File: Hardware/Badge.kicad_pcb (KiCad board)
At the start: 2 copper layers, 100 x 100 mm, 128 parts, among them IC2 ST25DV04K-IER6S3, J1 Battery_Conn, J4 Conn_02x15_Counter_Clockwise, J5 Conn_01x12, J6 Internal_I2C, P1 USB_C_Plug_USB2.0, P2 ESP_DATA, Q1 SI1967DH-T1-GE3, Q2 2SC4213, SW1 BOOT_MODE, SW2 RESET, SW3 PWR_BATT, SW4 ESP_BOOT, SW5 Button B, SW6 Button A, SW7 ESP_RST, U1 W25Q128JVS, U2 MCP73832-2-OT, U3 LD1117S33TR_SOT223, U4 RP2040, U5 BHI160B, U6 BMM150, U7 ESP32-S3-WROOM-1, X1 Simple_Addon_v2, Y1 12MHz_GND24

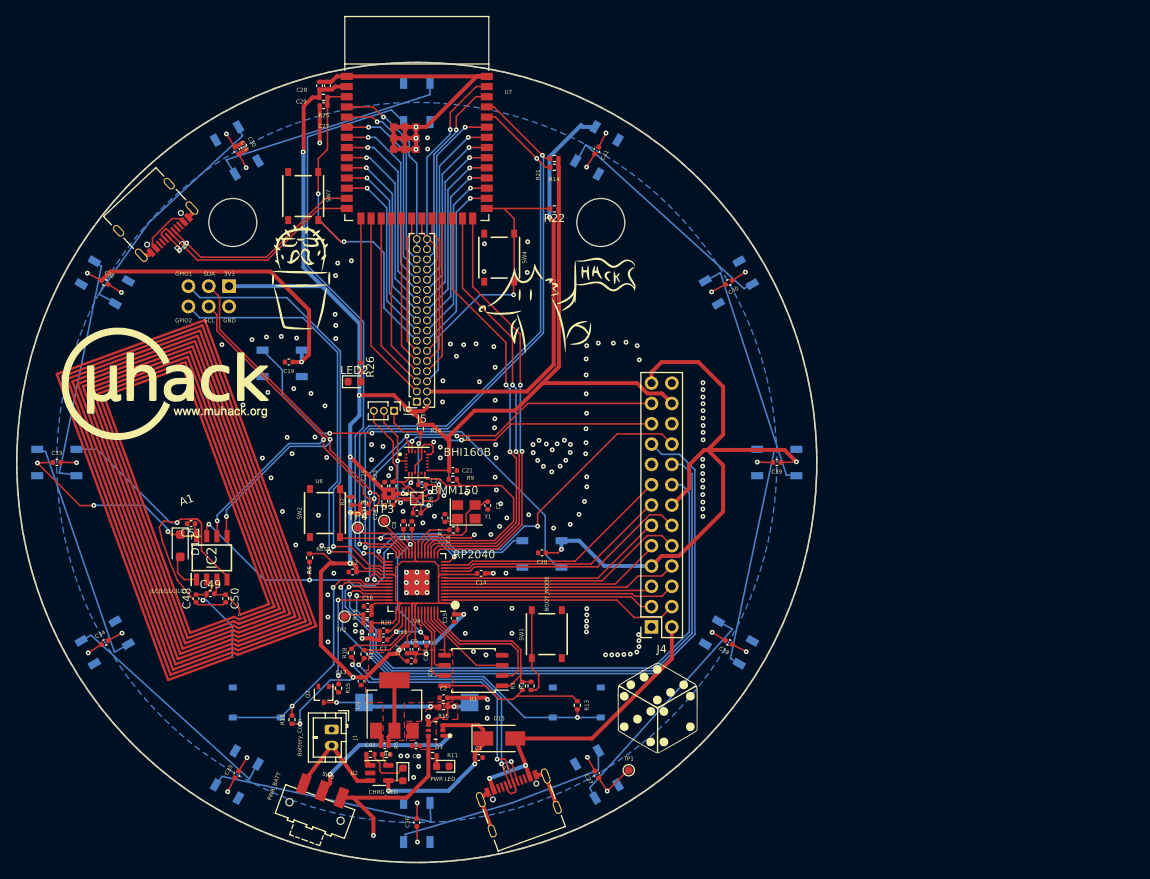
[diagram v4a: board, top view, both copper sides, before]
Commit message: TODO list completed - need to search for components
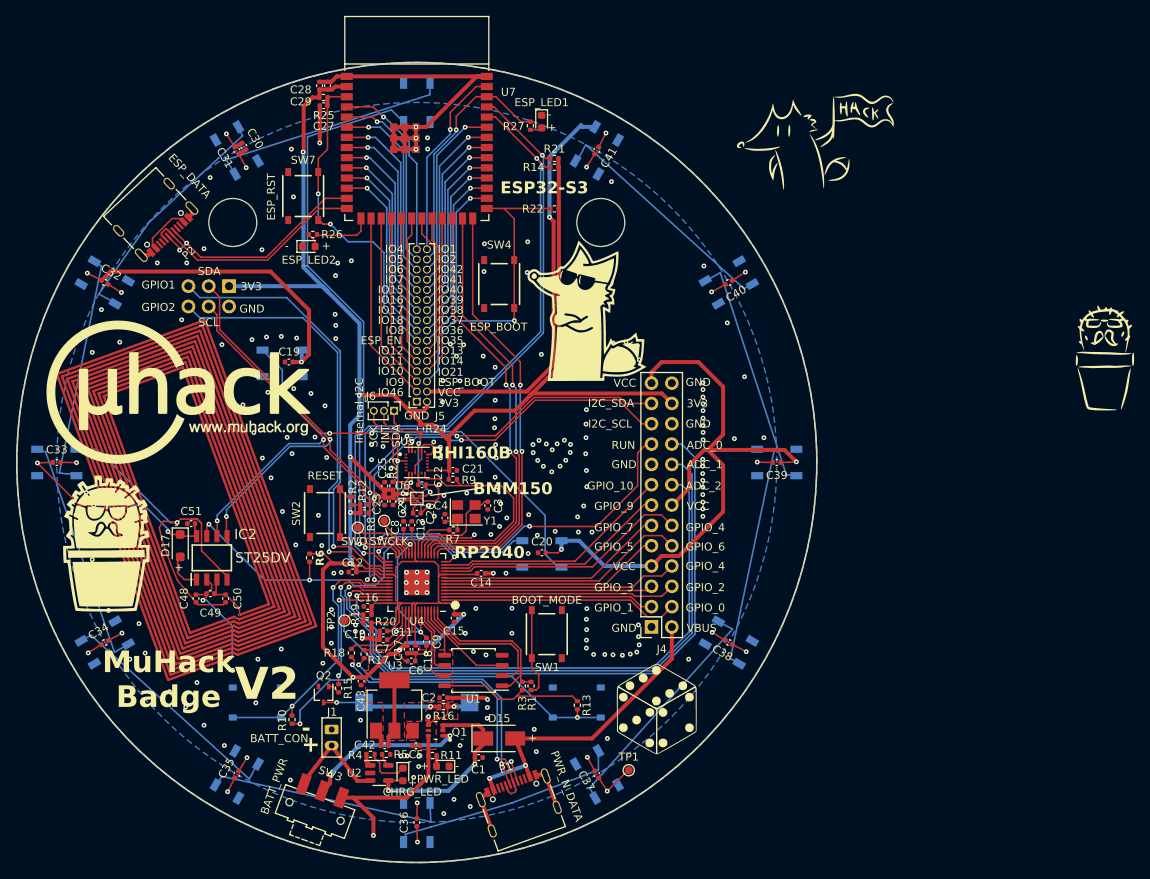
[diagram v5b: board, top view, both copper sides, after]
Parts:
- removed the G*** at (68.6, 90.2)
- added G***: LOGO, LOGO, F.Cu at (121.1, 81.1)
- added G***: LOGO, LOGO, F.Cu at (69.9, 91.2)
- added G***: LOGO, LOGO, F.Cu at (61.3, 110.1)
- added LED4: ESP_LED1, LED_SMD:LED_0603_1608Metric, F.Cu at (115.6, 57.4)
- added R27: 470, Resistor_SMD:R_0402_1005Metric, F.Cu at (114.2, 57.9)
- IC2: value ST25DV04K-IER6S3 -> ST25DV
- J1: value Battery_Conn -> BATT_CON
- J5: footprint Connector_PinSocket_1.27mm:PinSocket_2x17_P1.27mm_Vertical -> Connector_PinSocket_1.27mm:PinSocket_2x16_P1.27mm_Vertical
- LED2: value ESP LED -> ESP_LED2
- LED3: value PWR LED -> PWR_LED
- P1: value USB_C_Plug_USB2.0 -> PWR_N_DATA
- SW3: value PWR_BATT -> BATT_PWR
- TP3: value TestPoint -> SWCLK
- TP4: value TestPoint -> SWD
- U7: value ESP32-S3-WROOM-1 -> ESP32-S3
- X1: value Simple_Addon_v2 -> SAO_v2
- moved G*** 101.0 mm to (185.4, 86.9)
- moved G*** 38.3 mm to (149.8, 59.9)
- moved LED2 17.8 mm to (86.5, 73.0)
- moved R26 17.6 mm to (87.0, 71.5), turned to 180 degrees
- moved SW4 3.30 mm to (110.3, 77.7)
- moved TP2 0.50 mm to (91.0, 119.8)
- moved G*** 0.16 mm to (130.0, 130.8)
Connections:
- J4 pad 19: /ADC_0 -> /RUN
- J4 pad 20: /RUN -> /ADC_0
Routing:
- net /WiFi_BT/IO3: track 18.0 -> 7.34 mm
- net /WiFi_BT/IO2: track 24.2 -> 31.0 mm
- net /ESP_EN: track 45.2 -> 42.6 mm
- net /I2C_SCL: track 107.9 -> 110.4 mm
- net /RUN: track 61.8 -> 59.7 mm
- net /ESP_BOOT: track 37.3 -> 39.2 mm
- net /ADC_0: track 86.0 -> 84.4 mm
- net Net-(LED4-A): track 0.00 -> 1.49 mm
- net +3V3: track 341.4 -> 342.1 mm
- net /I2C_SDA: track 116.1 -> 116.7 mm
- net GND: vias 183 -> 239
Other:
- board text added: "+"
- board text added: "-"
- board text added: "3V3"
- board text added: "ADC_0"
- board text added: "ADC_1"
- board text added: "ADC_2"
- board text added: "ESP_BOOT"
- board text added: "ESP_EN"
- board text added: "GND"
- board text added: "GPIO_0"
- board text added: "GPIO_1"
- board text added: "GPIO_10"
- board text added: "GPIO_2"
- board text added: "GPIO_3"
- board text added: "GPIO_4"
- board text added: "GPIO_5"
- board text added: "GPIO_6"
- board text added: "GPIO_7"
- board text added: "GPIO_9"
- board text added: "I2C_SCL"
- board text added: "I2C_SDA"
- board text added: "INT"
- board text added: "IO1"
- board text added: "IO10"
- board text added: "IO11"
- board text added: "IO12"
- board text added: "IO13"
- board text added: "IO14"
- board text added: "IO15"
- board text added: "IO16"
- board text added: "IO17"
- board text added: "IO18"
- board text added: "IO2"
- board text added: "IO21"
- board text added: "IO35"
- board text added: "IO36"
- board text added: "IO37"
- board text added: "IO38"
- board text added: "IO39"
- board text added: "IO4"
- board text added: "IO40"
- board text added: "IO41"
- board text added: "IO42"
- board text added: "IO46"
- board text added: "IO5"
- board text added: "IO6"
- board text added: "IO7"
- board text added: "IO8"
- board text added: "IO9"
- board text added: "MuHack Badge"
- board text added: "RUN"
- board text added: "SCK"
- board text added: "SDA"
- board text added: "V2"
- board text added: "VBUS"
- board text added: "VCC"
- board text removed: "JLCJLCJLCJLC"

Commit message: Testing with different power circuit
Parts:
- removed the G*** at (185.4, 86.9)
- removed the G*** at (149.8, 59.9)

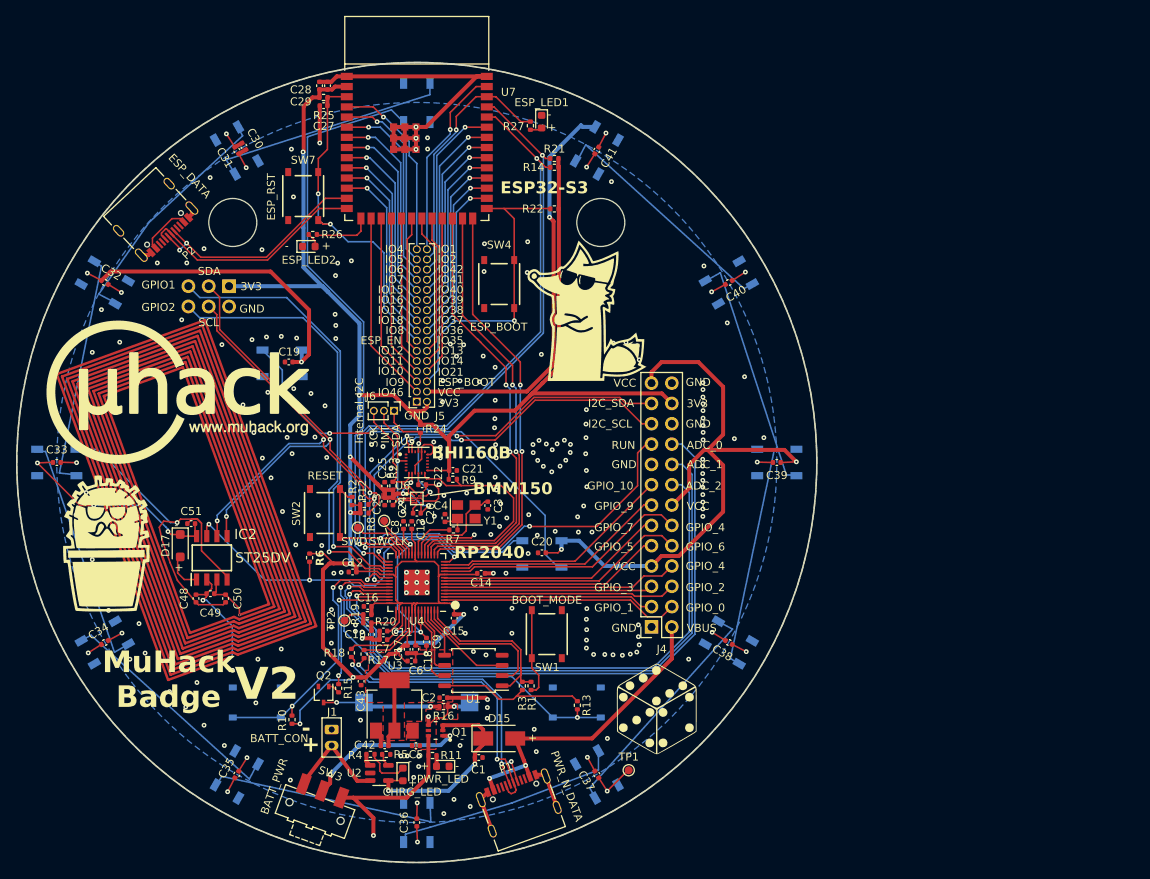
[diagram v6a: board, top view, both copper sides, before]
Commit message: Ready to order - THE POWER DIODE IS MISSING (need futher investigations)
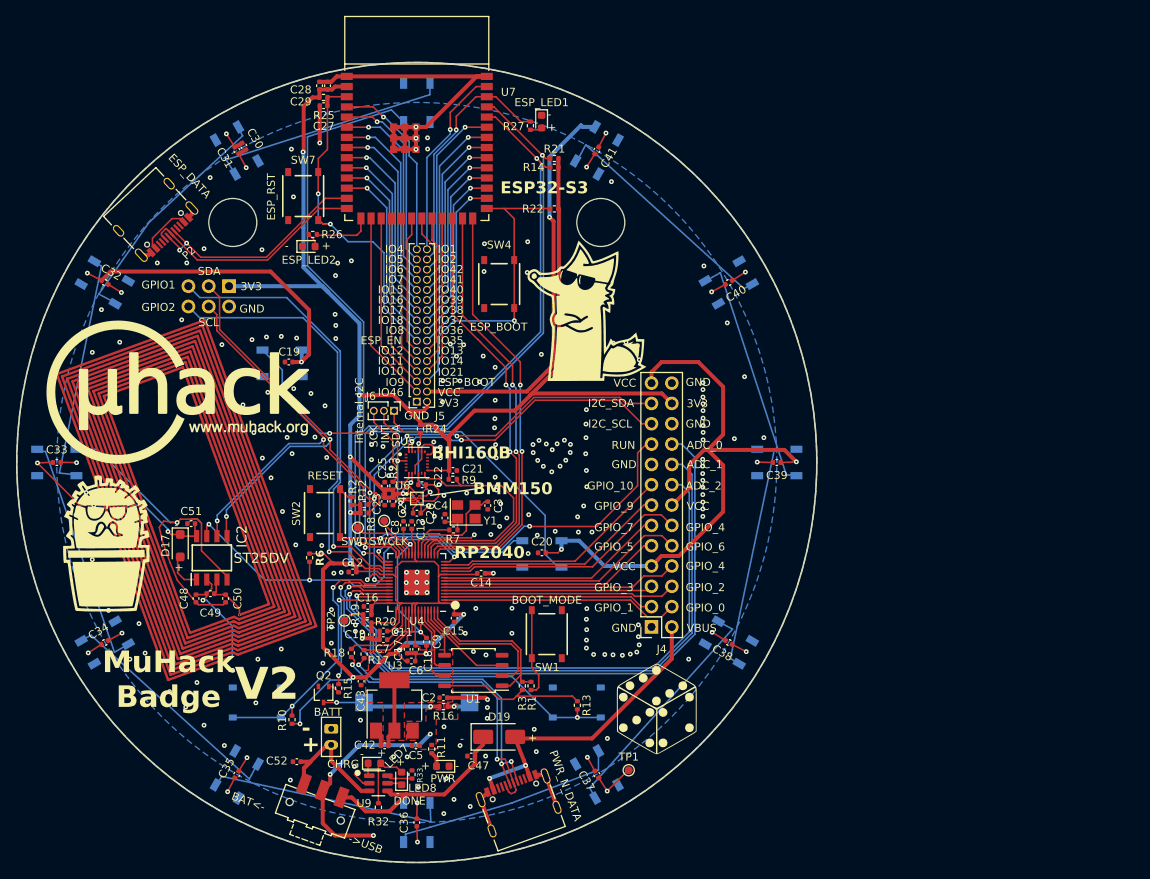
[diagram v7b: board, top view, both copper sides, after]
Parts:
- removed C1: 100n, Capacitor_SMD:C_0402_1005Metric
- removed D15: D_Schottky, Diode_SMD:D_SMA
- removed J1: BATT_CON, Connector_JST:JST_PH_B2B-PH-K_1x02_P2.00mm_Vertical
- removed LED1: CHRG_LED, LED_SMD:LED_0603_1608Metric
- removed P1: PWR_N_DATA, Connector_USB:USB_C_Receptacle_Palconn_UTC16-G
- removed Q1: SI1967DH-T1-GE3, SI1967DH:Vishay-S-03946-07_2001-B-0
- removed R4: 1k, Resistor_SMD:R_0402_1005Metric
- removed R5: 2k, Resistor_SMD:R_0402_1005Metric
- removed SW3: BATT_PWR, Button_Switch_SMD:SW_SPDT_CK-JS102011SAQN
- removed U2: MCP73832-2-OT, Package_TO_SOT_SMD:SOT-23-5
- added BT1: BATT, Connector_JST:JST_PH_B2B-PH-K_1x02_P2.00mm_Vertical, F.Cu at (89.3, 133.3)
- added C47: 4.7uF, Capacitor_SMD:C_0402_1005Metric, F.Cu at (106.8, 136.7)
- added C52: 4.7uF, Capacitor_SMD:C_0402_1005Metric, F.Cu at (85.0, 137.4)
- added D19: D_Schottky, Diode_SMD:D_SMA, F.Cu at (110.3, 134.3)
- added LED7: CHRG, LED_SMD:LED_0603_1608Metric, F.Cu at (94.7, 137.6)
- added LED8: DONE, LED_SMD:LED_0603_1608Metric, F.Cu at (98.1, 139.5)
- added P4: PWR_N_DATA, Connector_USB:USB_C_Receptacle_Palconn_UTC16-G, F.Cu at (112.7, 142.5)
- added R32: 1k, Resistor_SMD:R_0402_1005Metric, F.Cu at (95.2, 143.1)
- added R33: 2k, Resistor_SMD:R_0402_1005Metric, F.Cu at (99.4, 139.0)
- added SW9: PWR_SWT, Button_Switch_SMD:SW_SPDT_CK-JS102011SAQN, F.Cu at (87.3, 143.6)
- added U9: TP4057, Package_TO_SOT_SMD:SOT-23-6, F.Cu at (95.2, 140.1)
- LED3: value PWR_LED -> PWR
- moved R11 0.82 mm to (101.9, 135.8), turned to -90 degrees
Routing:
- net Net-(D15-K): track 26.1 -> 0.00 mm, vias 2 -> 0
- net Net-(D19-K): track 0.00 -> 26.0 mm
- net Net-(Q1A-S1): track 21.4 -> 0.00 mm, vias 2 -> 0
- net Net-(BT1-+): track 0.00 -> 17.2 mm
- net Net-(J1-Pin_2): track 13.4 -> 0.00 mm
- net Net-(LED7-A): track 0.00 -> 8.18 mm
- net +3V3: track 342.1 -> 336.4 mm
- net Net-(LED1-K): track 5.60 -> 0.00 mm
- net Net-(U9-PROG): track 0.00 -> 3.21 mm
- net GND: track 182.5 -> 184.6 mm, vias 239 -> 240
- net Net-(LED8-K): track 0.00 -> 1.84 mm
- net Net-(LED7-K): track 0.00 -> 1.61 mm
- net Net-(U2-PROG): track 1.58 -> 0.00 mm
- net Net-(U2-STAT): track 1.58 -> 0.00 mm
- net Net-(C4-Pad2): track 3.61 -> 2.66 mm
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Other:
- board text added: "->USB"
- board text added: "BAT<-"

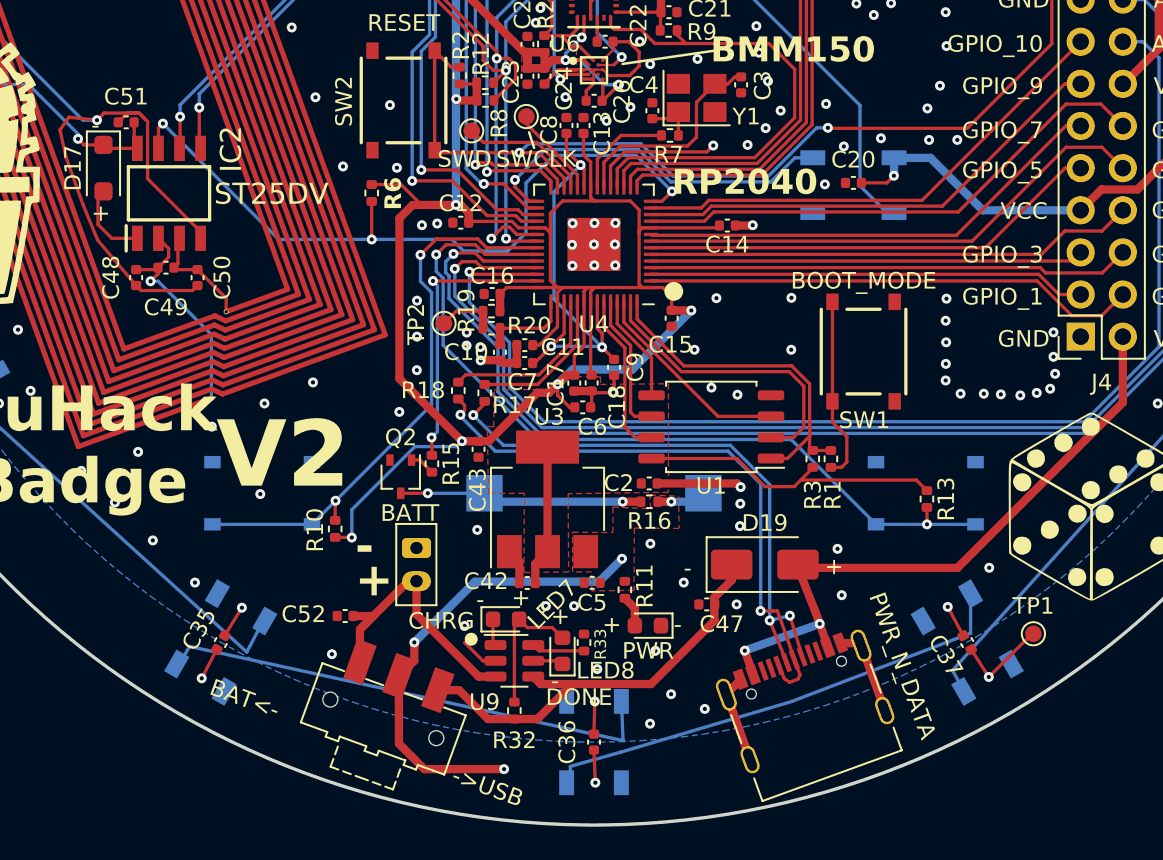
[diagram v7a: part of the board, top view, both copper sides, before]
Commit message: Reworked the power system - ORDERED ON JLCPCB
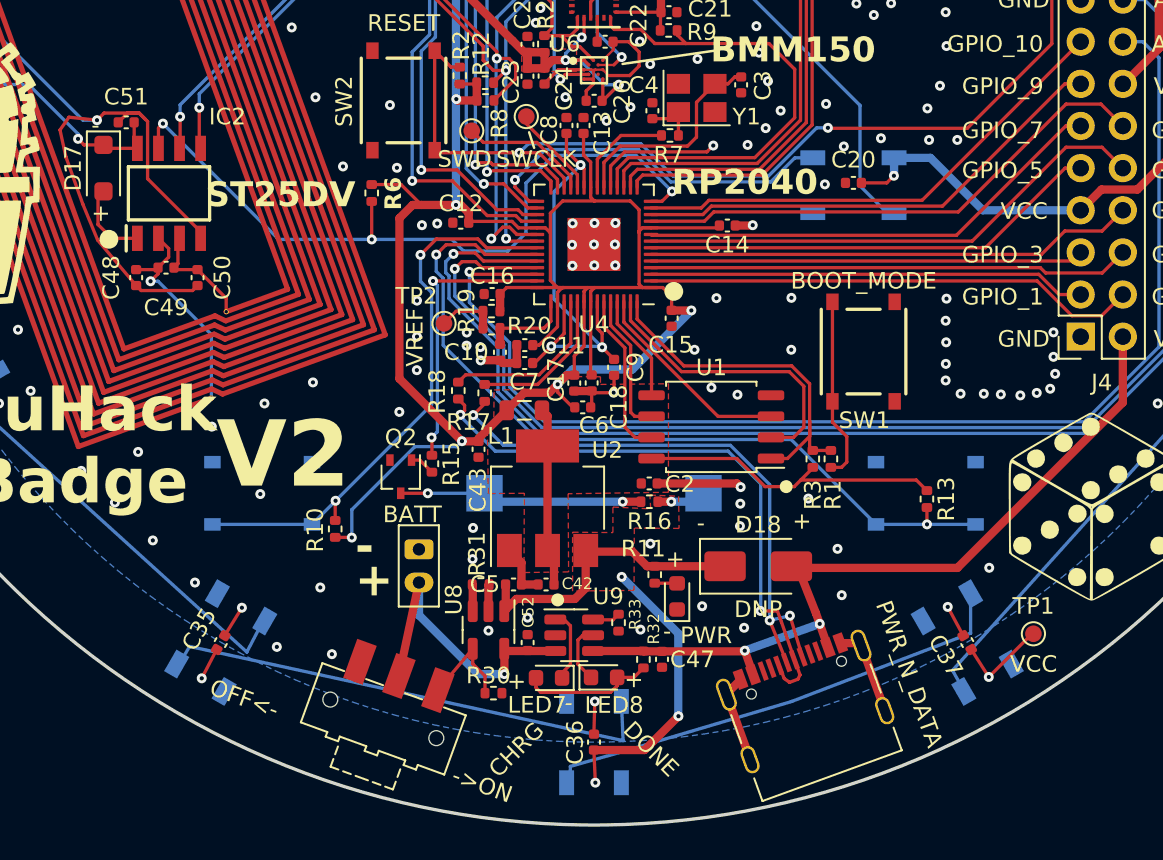
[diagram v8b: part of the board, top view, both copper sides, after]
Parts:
- removed D19: D_Schottky, Diode_SMD:D_SMA
- removed P4: PWR_N_DATA, Connector_USB:USB_C_Receptacle_Palconn_UTC16-G
- removed U3: LD1117S33TR_SOT223, Package_TO_SOT_SMD:SOT-223-3_TabPin2
- added D18: DNP, Diode_SMD:D_SMA, F.Cu at (109.9, 134.4)
- added L1: 2.2uH, Inductor_SMD:L_0805_2012Metric, F.Cu at (95.8, 125.0)
- added P1: PWR_N_DATA, Connector_USB:USB_C_Receptacle_Palconn_UTC16-G, F.Cu at (112.7, 142.5)
- added R30: 100k, Resistor_SMD:R_0402_1005Metric, F.Cu at (93.9, 142.1)
- added R31: 4.7k, Resistor_SMD:R_0402_1005Metric, F.Cu at (93.2, 135.5)
- added U2: AMS1117-3.3, Package_TO_SOT_SMD:SOT-223-3_TabPin2, F.Cu at (97.2, 130.3)
- added U8: SY6280AAC, Package_TO_SOT_SMD:SOT-23-5, F.Cu at (93.6, 138.2)
- C48, C49, C50: value NC -> DNP
- TP1: value TestPoint -> VCC
- TP2: value TestPoint -> VREF
- moved C52 11.1 mm to (96.0, 139.0), turned to 90 degrees
- moved R32 8.37 mm to (103.0, 140.0), turned to 90 degrees
- moved C5 4.74 mm to (95.2, 135.5), turned to 180 degrees
- moved LED7 4.38 mm to (97.3, 141.1), turned to 180 degrees
- moved C47 4.27 mm to (104.1, 140.0), turned to -90 degrees
- moved U9 3.92 mm to (98.8, 138.6)
- moved LED8 2.98 mm to (100.6, 141.1), turned to 0 degrees
- moved LED3 2.49 mm to (105.0, 136.2), turned to 90 degrees
- moved R33 2.40 mm to (101.5, 137.8), turned to 90 degrees
- moved R11 2.02 mm to (103.7, 134.9)
- moved C42 1.13 mm to (97.1, 135.5)
- moved BT1 0.17 mm to (89.5, 133.4)
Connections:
- C42 pad 2: +3V3 -> Net-(U2-VO)
- C47 pad 1: Net-(D19-K) -> VBUS
- R32 pad 2: Net-(D19-K) -> VBUS
- SW9 pad 1: Net-(D19-K) -> Net-(SW9-A)
- SW9 pad 2: VCC -> Net-(BT1-+)
- SW9 pad 3: Net-(BT1-+) -> unconnected-(SW9-C-Pad3)
- U9 pad 4: Net-(D19-K) -> VBUS
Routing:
- net Net-(D19-K): track 26.0 -> 0.00 mm
- net Net-(U2-VO): track 0.00 -> 10.9 mm
- net +3V3: track 336.4 -> 327.2 mm
- net VBUS: track 39.2 -> 48.3 mm
- net Net-(SW9-A): track 0.00 -> 6.24 mm
- net VCC: track 249.7 -> 255.5 mm, vias 20 -> 19
- net Net-(LED7-K): track 1.61 -> 4.42 mm
- net Net-(BT1-+): track 17.2 -> 19.7 mm, vias 0 -> 1
- net Net-(LED8-K): track 1.84 -> 3.61 mm
- net Net-(U8-SET): track 0.00 -> 1.61 mm
- net Net-(U9-PROG): track 3.21 -> 1.69 mm
- net Net-(LED3-A): track 1.90 -> 1.36 mm
- net GND: track 184.6 -> 185.1 mm, vias 240 -> 239
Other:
- board text added: "->ON"
- board text added: "OFF<-"
- board text removed: "->USB"
- board text removed: "BAT<-"
